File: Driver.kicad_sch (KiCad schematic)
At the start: 40 parts

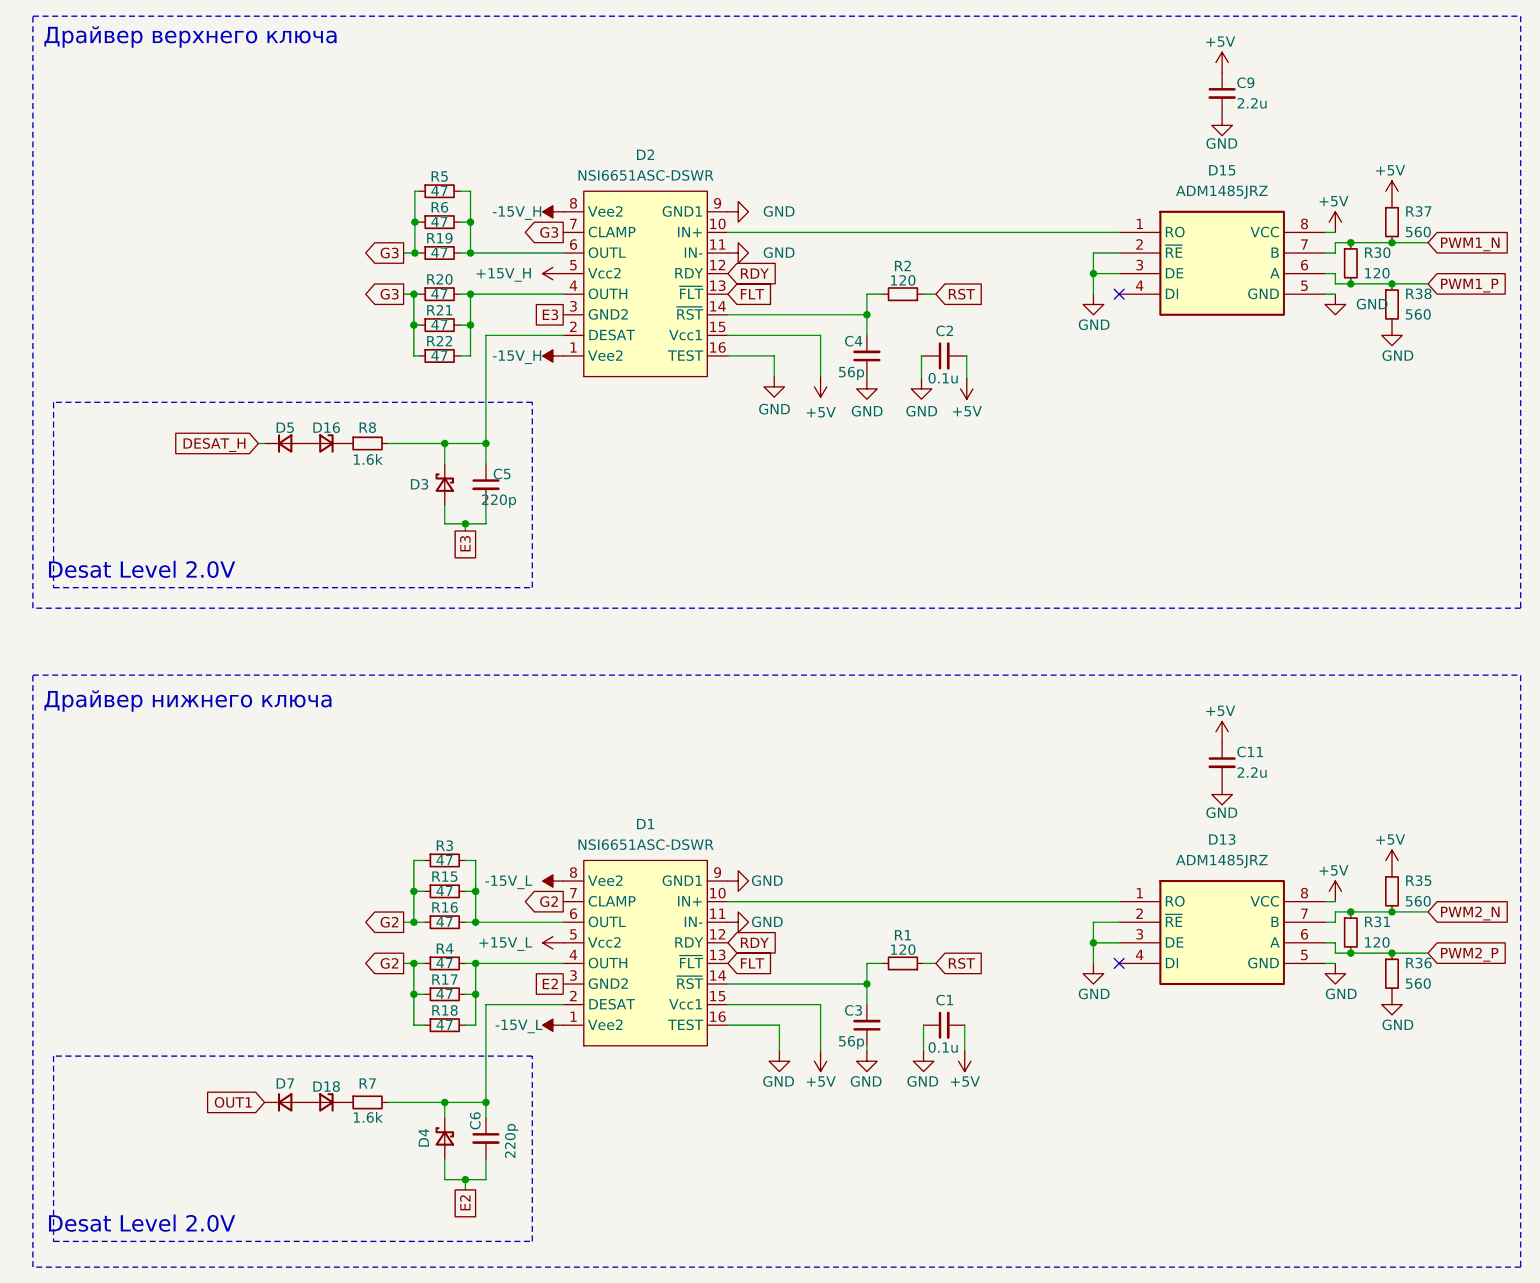
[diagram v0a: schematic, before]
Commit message: VER2_Test: добавил новый BOM и в схеме заменил названия компонентов
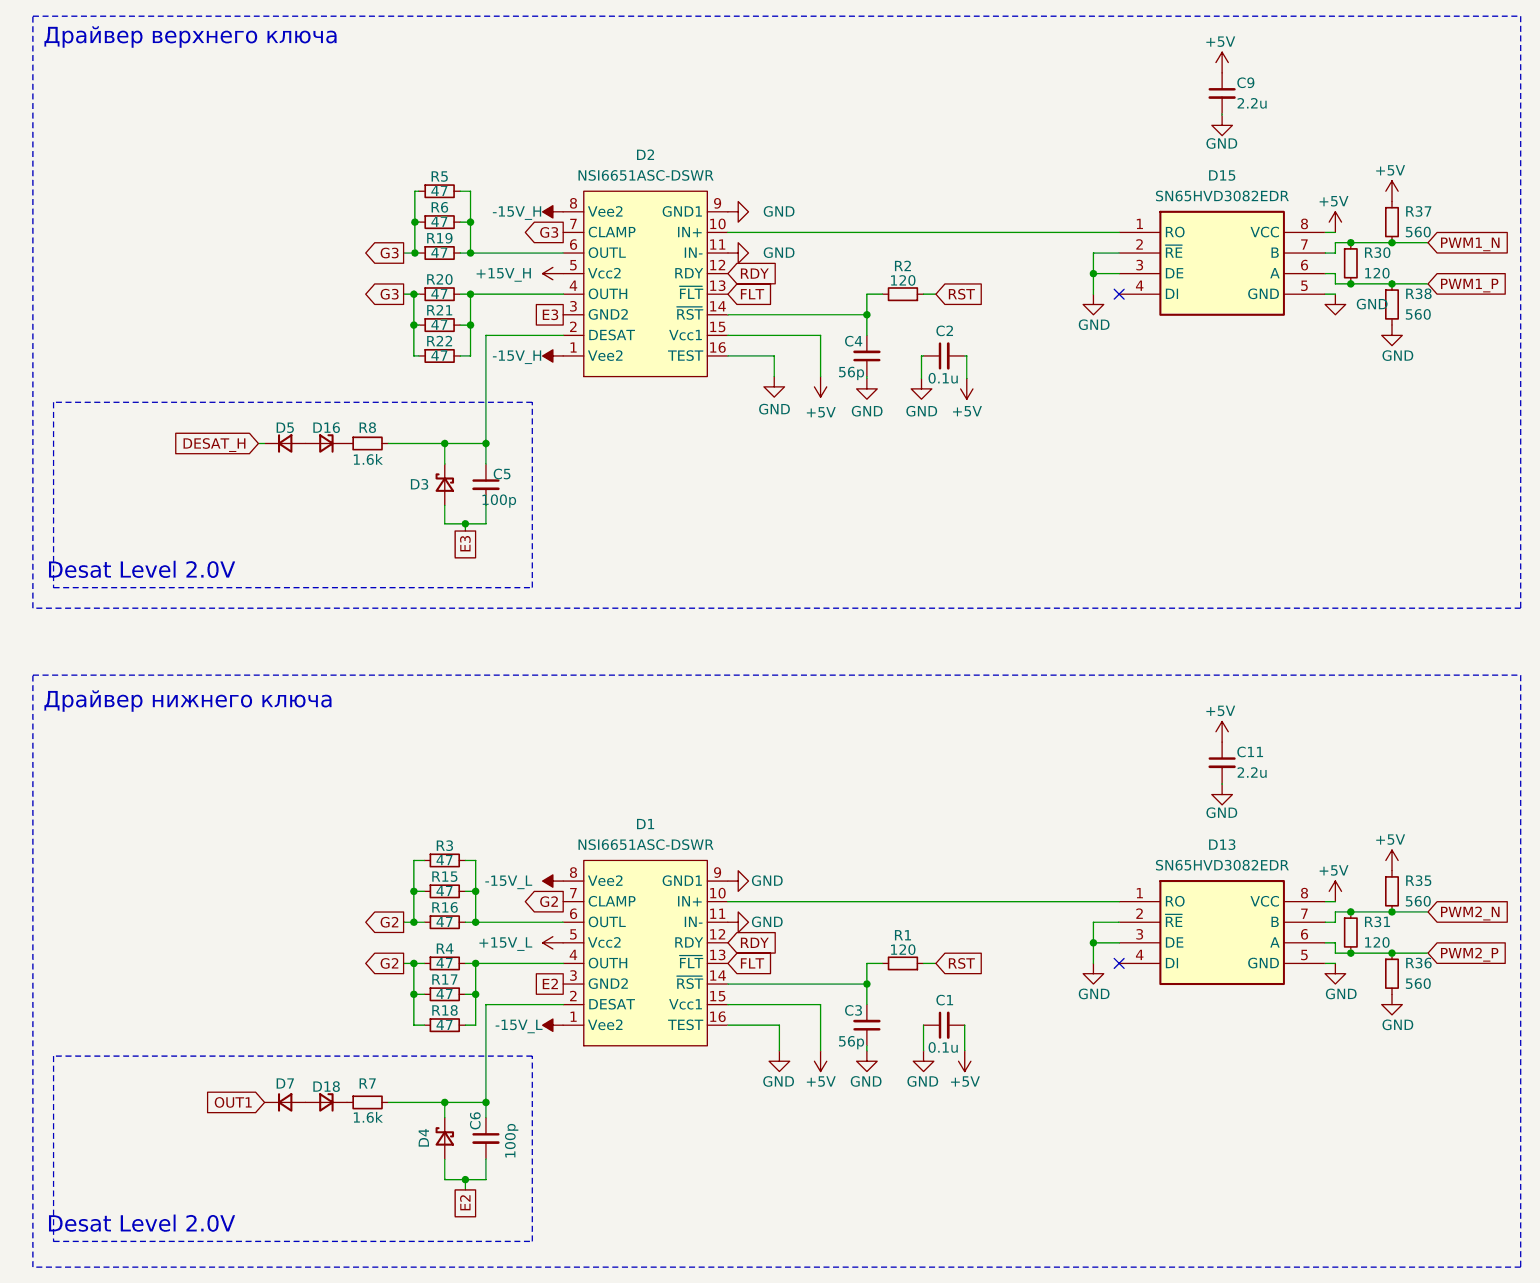
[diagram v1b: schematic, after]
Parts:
- C5, C6: value 220p -> 100p
- D13, D15: value ADM1485JRZ -> SN65HVD3082EDR
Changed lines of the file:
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@@
 			)
 		)
-		(property "Value" "220p"
+		(property "Value" "100p"
 			(at 176.53 121.285 0)
 			(effects
@@
 		(fields_autoplaced yes)
 		(property "Reference" "D13"
-			(at 263.525 163.195 0)
+			(at 263.525 163.83 0)
 			(effects
 				(font
@@
 			)
 		)
-		(property "Value" "ADM1485JRZ"
-			(at 263.525 165.735 0)
+		(property "Value" "SN65HVD3082EDR"
+			(at 263.525 166.37 0)
 			(effects
 				(font
@@
 			)
 		)
-		(property "Value" "220p"
+		(property "Value" "100p"
 			(at 175.768 202.565 90)
 			(effects
@@
 		(fields_autoplaced yes)
 		(property "Reference" "D15"
-			(at 263.525 80.645 0)
+			(at 263.525 81.28 0)
 			(effects
 				(font
@@
 			)
 		)
-		(property "Value" "ADM1485JRZ"
-			(at 263.525 83.185 0)
+		(property "Value" "SN65HVD3082EDR"
+			(at 263.525 83.82 0)
 			(effects
 				(font
